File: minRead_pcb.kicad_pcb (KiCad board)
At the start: 2 copper layers, 60 x 111.3 mm, 174 parts, among them J1 USB_C_Receptacle, J2 FH34SRJ-24S-0.5SH_50_, J3 FH34SRJ-6S-0.5SH_50_, J4 FH34SRJ-6S-0.5SH_50_, J5 Conn_01x02, J6 PPPC062LJBN-RC, J7 Micro_SD_Card, Q1 FS8205A, Q3 AO3419, Q4 BSS138, Q5 BSS138, Q6 BSS138, Q7 AO3419, Q8 AO3419, SW1 SW_Push, SW10 SW_Push, SW11 SW_Push, SW2 SW_Push, SW3 SW_Push, SW4 SW_Push, SW5 SW_Push, SW6 SW_Push, SW7 SW_Push, SW8 SW_Push, SW9 SW_Push, U1 TPD4E1U06DBVR, U10 TPS923610DRLR, U11 TP4056-42-ESOP8, U12 74LVC1G04, U13 DS3231MZ, U2 TPS2116DRL, U3 AP2112K-3.3, U4 ESP32-S3-WROOM-1, U5 DW01A, U6 TPD4E1U06DBVR, U7 TPD4E1U06DBVR, U8 TPD4E1U06DBVR, U9 TPD4E1U06DBVR

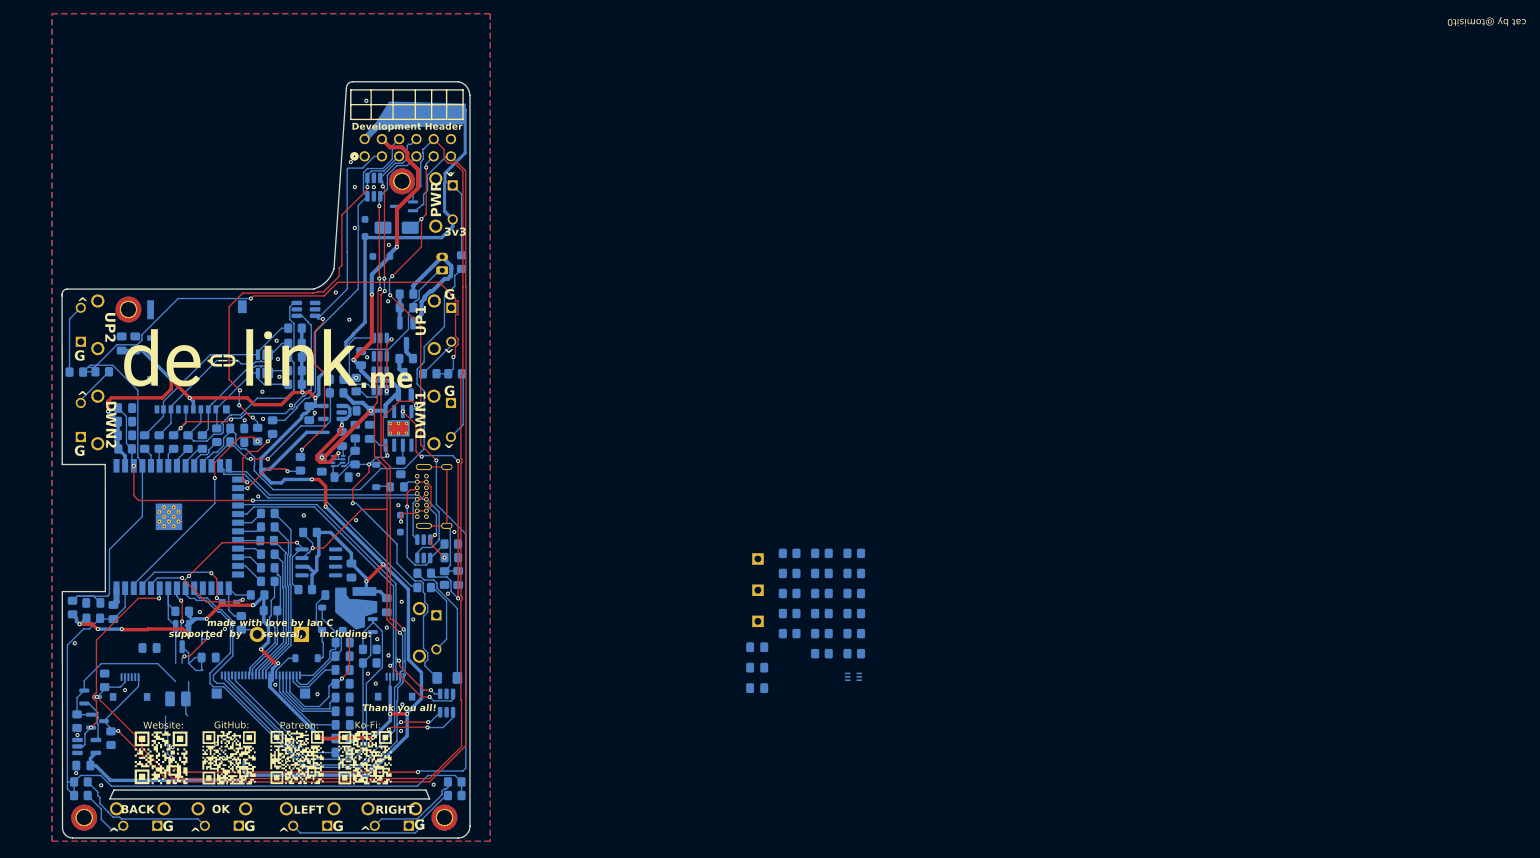
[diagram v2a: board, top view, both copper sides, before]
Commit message: Downsize passives to 0603, document D1 redundancy and layout guidance
Schematic:
- Swap 78 resistors and 22 capacitors from 0805 to 0603 hand-solder
  footprints, recovering ~228 mm^2 of courtyard. F1 (fuse) and D2 (LED)
  untouched. 13 capacitors deliberately kept at 0805.
- C11 and C17 annotated /50V, closing the HV cap rating gap.

DESIGN_REVIEW.md:
- 6.19: 0805->0603 migration audit. Corrected an earlier power analysis
  that wrongly assumed full rail voltage across every resistor; real
  worst case is R14 at 28 mW (28% of an 0603). Verified 0603 MLCC
  ceilings against manufacturer catalogs and LCSC stock: 4.7uF/50V does
  not exist in 0603, and 22uF/6.3V delivers only 6.7uF at 3.3V bias.
- 6.20: D1 (series Schottky on VBUS) is redundant. TPS2116 specifies
  1 nA reverse leakage out of an unselected input; the TP4056 datasheet
  states outright that no blocking diode is required. D1 costs 0.3-0.6 V
  of headroom, exceeds its SOD-123 500 mW rating at the current F1 will
  pass, and blocks raising R38 to close the LDO brown-out window.
- 3.3: withdrew the earlier "raise C9 to 4.7uF" recommendation. Ripple
  at 1.1 MHz is optically invisible and R37 dominates the loop, while
  larger C9 slows CCT blending worst at low brightness. 1 uF is correct.
- 8: new placement and layout guidance for the 2-layer stackup, covering
  the two switching loops, thermal separation of U3/U11, analog routing,
  and the antenna keepout.

docs/HARDWARE.md:
- Note D1 under review; document the 0603/0805 split and its rationale.

Add .gitignore rules for KiCad autosave, lock and backup files.

ERC: 0 errors, 40 cosmetic warnings. Netlist verified at 170 components
and 127 nets after the footprint swap.
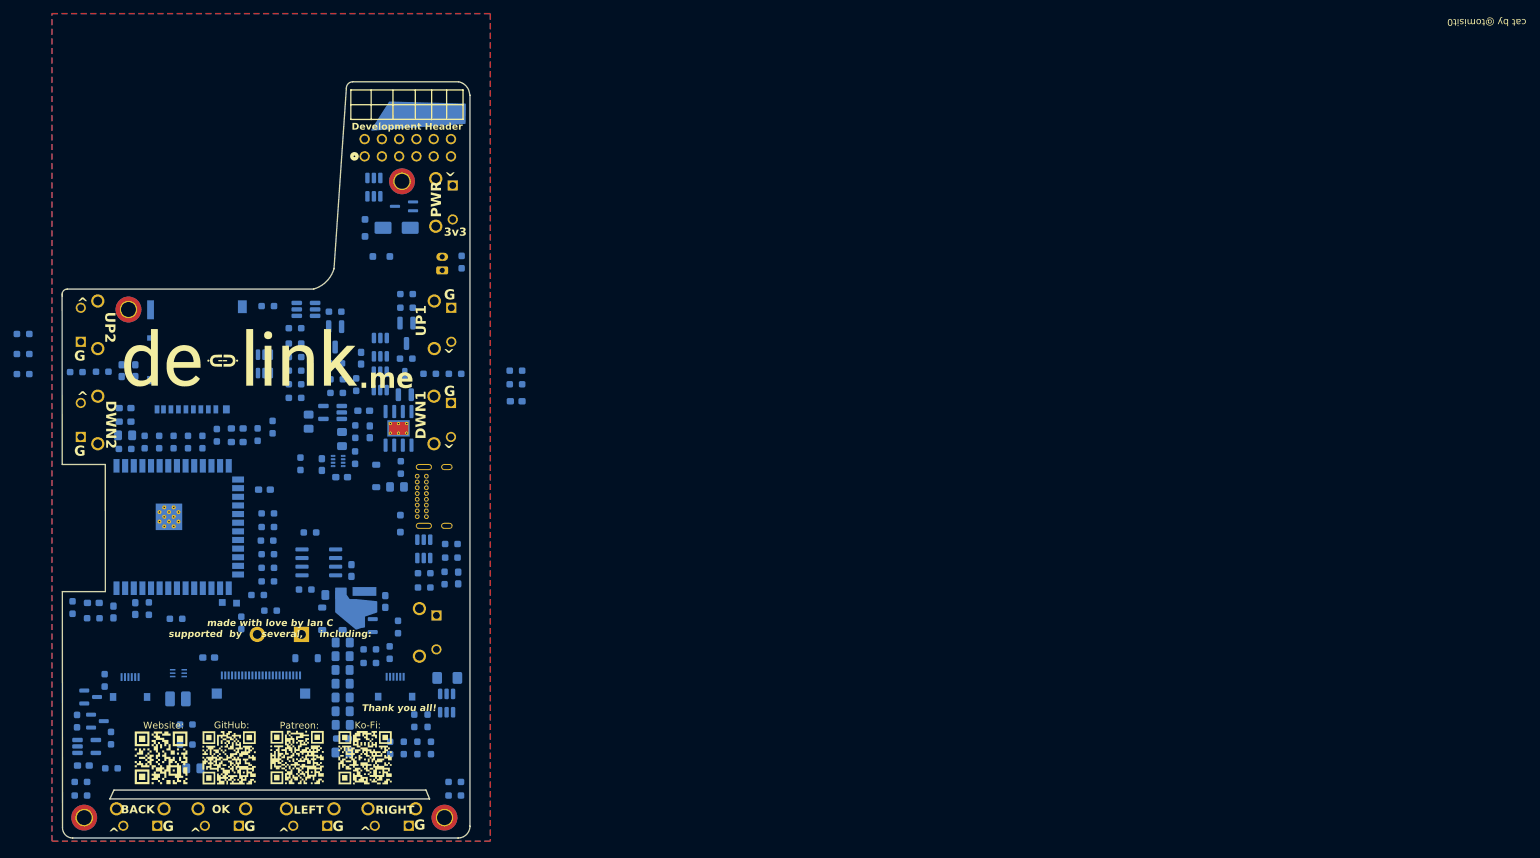
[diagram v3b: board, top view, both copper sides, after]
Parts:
- removed TP3, TP4, TP5: TestPoint, Connector_PinHeader_2.54mm:PinHeader_1x01_P2.54mm_Vertical
- added R75: 100k, Resistor_SMD:R_0603_1608Metric_Pad0.98x0.95mm_HandSolder, B.Cu at (51.5, 138.0)
- added R76: 100k, Resistor_SMD:R_0603_1608Metric_Pad0.98x0.95mm_HandSolder, B.Cu at (74.5, 70.0)
- added R77: 100k, Resistor_SMD:R_0603_1608Metric_Pad0.98x0.95mm_HandSolder, B.Cu at (78.5, 83.5)
- added R78: 1k, Resistor_SMD:R_0603_1608Metric_Pad0.98x0.95mm_HandSolder, B.Cu at (84.5, 78.4)
- C1, C10, C12, C2, C21, C22, C23, C24, C25, C26, C27, C28, C29, C3, C30, C33, C36, C5, C7, C8: footprint Capacitor_SMD:C_0805_2012Metric_Pad1.18x1.45mm_HandSolder -> Capacitor_SMD:C_0603_1608Metric_Pad1.08x0.95mm_HandSolder
- C13, C14, C15, C16: value 4.7u -> 4.7u/50V
- C20, C9: value 1u -> 1u/50V
- C31: value 10n -> 100n; footprint Capacitor_SMD:C_0805_2012Metric_Pad1.18x1.45mm_HandSolder -> Capacitor_SMD:C_0603_1608Metric_Pad1.08x0.95mm_HandSolder
- C37: value 4.7u -> 1u; footprint Capacitor_SMD:C_0805_2012Metric_Pad1.18x1.45mm_HandSolder -> Capacitor_SMD:C_0603_1608Metric_Pad1.08x0.95mm_HandSolder
- D3: value SMAJ30A -> SMAJ26A
- R1, R10, R11, R12, R13, R14, R15, R16, R18, R19, R2, R20, R21, R22, R23, R24, R25, R26, R27, R28, R29, R3, R30, R31, R32, R33, R34, R35, R36, R37, R39, R4, R40, R41, R42, R43, R44, R45, R46, R49, R5, R50, R51, R52, R53, R54, R55, R58, R59, R6, R60, R61, R62, R63, R64, R65, R66, R67, R68, R69, R7, R70, R71, R72, R73, R74, R8, R9: footprint Resistor_SMD:R_0805_2012Metric_Pad1.20x1.40mm_HandSolder -> Resistor_SMD:R_0603_1608Metric_Pad0.98x0.95mm_HandSolder
- R17: value 100k -> 150k; footprint Resistor_SMD:R_0805_2012Metric_Pad1.20x1.40mm_HandSolder -> Resistor_SMD:R_0603_1608Metric_Pad0.98x0.95mm_HandSolder
- R38: value 310k -> 240k; footprint Resistor_SMD:R_0805_2012Metric_Pad1.20x1.40mm_HandSolder -> Resistor_SMD:R_0603_1608Metric_Pad0.98x0.95mm_HandSolder
- R47, R48: value 4.7k -> 2.2k; footprint Resistor_SMD:R_0805_2012Metric_Pad1.20x1.40mm_HandSolder -> Resistor_SMD:R_0603_1608Metric_Pad0.98x0.95mm_HandSolder
- R56: value 1k -> 10k; footprint Resistor_SMD:R_0805_2012Metric_Pad1.20x1.40mm_HandSolder -> Resistor_SMD:R_0603_1608Metric_Pad0.98x0.95mm_HandSolder
- R57: value 100k -> 1M; footprint Resistor_SMD:R_0805_2012Metric_Pad1.20x1.40mm_HandSolder -> Resistor_SMD:R_0603_1608Metric_Pad0.98x0.95mm_HandSolder
- moved R72 119.1 mm to (38.5, 74.1)
- moved R73 119.1 mm to (38.5, 77.0)
- moved R74 119.1 mm to (38.5, 80.0)
- moved R39 100.7 mm to (62.5, 131.6)
- moved R41 100.7 mm to (62.5, 134.5)
- moved R17 100.2 mm to (61.0, 116.0)
- moved U10 99.3 mm to (61.4, 124.0)
- moved R70 94.6 mm to (57.0, 114.5), turned to -90 degrees
- moved C23 92.2 mm to (55.0, 114.5), turned to -90 degrees
- moved C9 84.8 mm to (63.5, 138.0)
- moved R43 70.3 mm to (92.5, 135.0), turned to 90 degrees
- moved R42 68.6 mm to (92.4, 121.0), turned to -90 degrees
- moved R44 67.2 mm to (93.7, 117.2), turned to -90 degrees
- moved R45 64.2 mm to (98.5, 135.0), turned to 90 degrees
- moved R66 63.8 mm to (94.5, 135.0), turned to 90 degrees
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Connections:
- C12 pad 2: Net-(Q7-D) -> LDO_IN
- C36 pad 2: 3V3 -> SD_VDD
- C37 pad 2: 3V3 -> SD_VDD
- J6 pad 12: GND -> P+
- J6 pad 4: I2C_SDA -> GND
- J6 pad 8: P+ -> I2C_SDA
- J7 pad 4: 3V3 -> SD_VDD
- L2 pad 1: Net-(Q7-D) -> LDO_IN
- Q7 pad 1: LED_ACTIVATE -> Net-(Q7-G)
- Q7 pad 3: Net-(Q7-D) -> SD_VDD
- R40 pad 1: LED_ACTIVATE -> Net-(Q7-G)
- R53 pad 2: 3V3 -> SD_VDD
- R54 pad 2: 3V3 -> SD_VDD
- R55 pad 2: 3V3 -> SD_VDD
- R8 pad 2: 3V3 -> SD_VDD
- R9 pad 2: 3V3 -> SD_VDD
- U10 pad 1: Net-(Q7-D) -> LDO_IN
- U4 pad 28: IO35_PSRAM -> unconnected-(U4-IO35-Pad28)
- U4 pad 29: IO36_PSRAM -> unconnected-(U4-IO36-Pad29)
- U4 pad 30: IO37_PSRAM -> unconnected-(U4-IO37-Pad30)
- U4 pad 34: LED_ACTIVATE -> SD_ACTIVATE
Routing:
- net 3V3: track 399.9 -> 0.00 mm, vias 21 -> 0
- net I2C_SCL: track 184.1 -> 0.00 mm, vias 8 -> 0
- net I2C_SDA: track 174.7 -> 0.00 mm, vias 7 -> 0
- net C-: track 169.9 -> 0.00 mm, vias 1 -> 0
- net W-: track 166.8 -> 0.00 mm, vias 1 -> 0
- net LED_SW: track 151.3 -> 0.00 mm, vias 7 -> 0
- net BUTTON_ADC_2: track 129.0 -> 0.00 mm, vias 2 -> 0
- net BUTTON_ADC_1: track 100.3 -> 0.00 mm
- net UNUSED_GPIO_46: track 85.7 -> 0.00 mm, vias 4 -> 0
- net PWR_BUTTON: track 74.0 -> 0.00 mm
- net P+: track 73.5 -> 0.00 mm, vias 5 -> 0
- net Net-(U4-IO46): track 70.7 -> 0.00 mm, vias 6 -> 0
- net USB_VBUS: track 70.3 -> 0.00 mm, vias 4 -> 0
- net ESP32_EN: track 61.2 -> 0.00 mm, vias 2 -> 0
- net TP_RST: track 54.4 -> 0.00 mm, vias 2 -> 0
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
